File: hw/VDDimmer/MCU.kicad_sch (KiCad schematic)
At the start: 22 parts, among them J1 USB-C 16P, J11 BTN1, J12 BTN2, J13 EXP 3V3/GND/SDA/SCL/EN/IO0, J14 UART1 3V3/GND/TX/RX, U1 ESP32-S3-WROOM-1U-N16

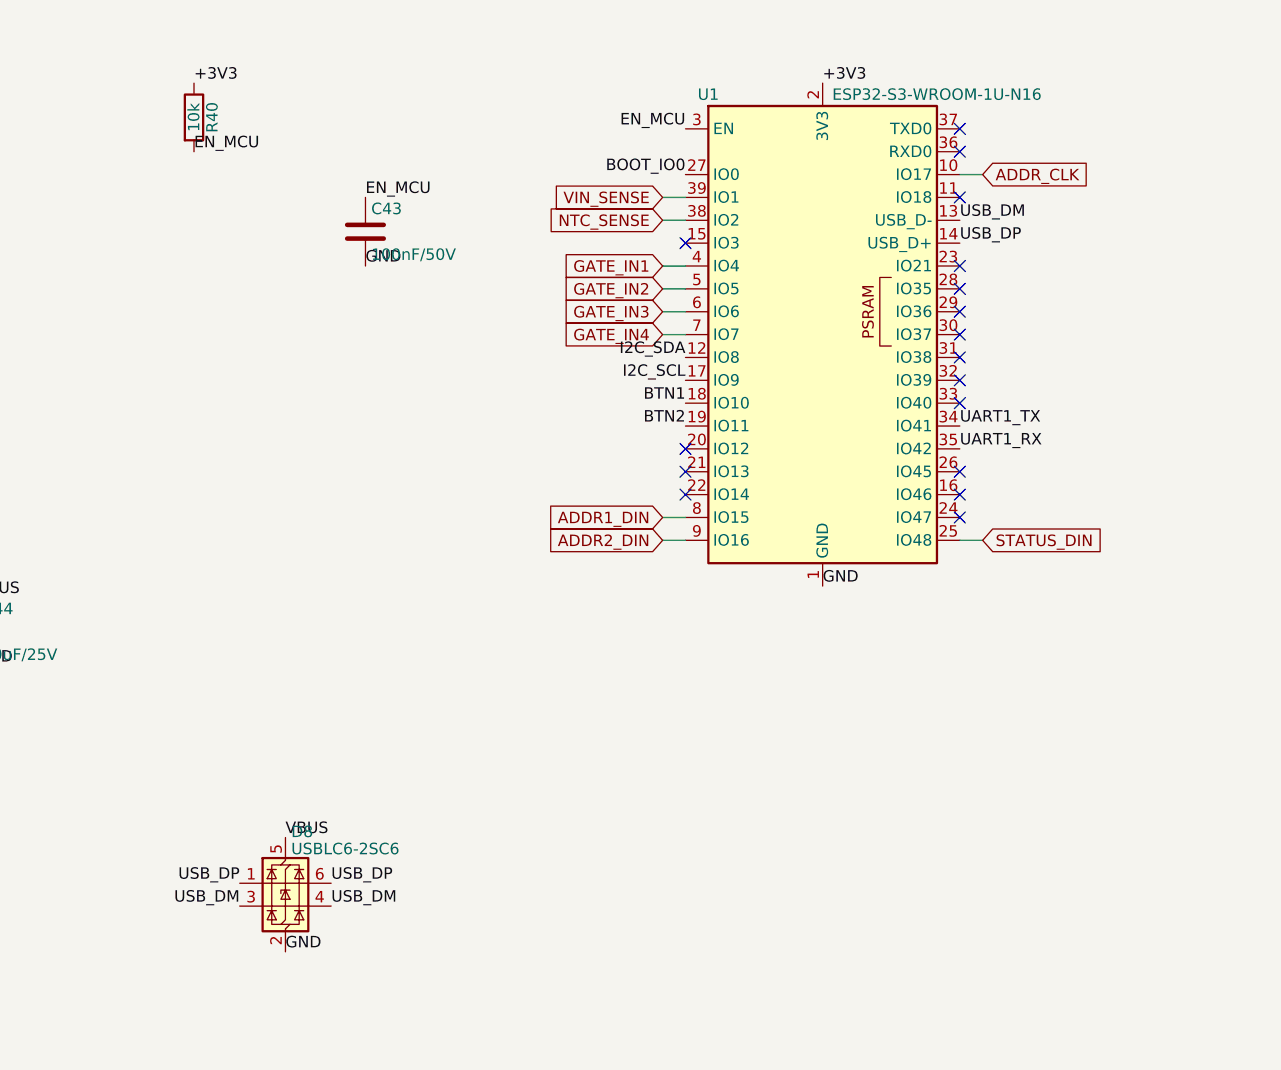
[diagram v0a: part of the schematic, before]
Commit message: Re-pin U1: move 8 nets off the bottom row onto free right-column GPIOs
Measured blocker: the escape from U1's bottom row past x=149.6 has a free
window of y 110.06..113.38 (3.32 mm) = 6 lanes at 0.25 mm trace / 0.2 mm
clearance, plus 3 more reachable via the D3-D4 slot into the corridor above Q4.
Nine eastbound nets left that row (GATE_IN1-4, ADDR1_DIN, ADDR2_DIN, ADDR_CLK,
I2C_SDA, EN_MCU) and four westbound returned through it (GDRV1-4): 13 needed,
9 available. Not routable on 2 layers with B.Cu reserved for GND.

Reassignment (schematic only, no BOM change, firmware-configurable):
  GATE_IN1  IO4  pad4  -> IO3   pad15   y 108.985
  GATE_IN2  IO5  pad5  -> IO46  pad16   y 107.715
  GATE_IN3  IO6  pad6  -> IO12  pad20   y 102.635
  GATE_IN4  IO7  pad7  -> IO13  pad21   y 101.365
  I2C_SDA   IO8  pad12 -> IO14  pad22   y 100.095  (level with J13.3)
  ADDR1_DIN IO15 pad8  -> IO21  pad23   y  98.825
  ADDR2_DIN IO16 pad9  -> IO47  pad24   y  97.555
  ADDR_CLK  IO17 pad10 -> IO45  pad26   y  95.015

Strapping-pin safety: IO45 (VDD_SPI select) and IO46 (ROM print control) both
drive 74HCT125 inputs only, which are high-Z, so their internal pulldowns hold
them low through reset. IO3 (JTAG source select) likewise sees only a high-Z
74HCT125 input, and its strap only selects JTAG routing. I2C_SDA, which may
carry an off-board pull-up via J13, went to IO14 -- not a strapping pin.

Corner load after: GDRV1-4 west (4) + EN_MCU east (1) = 5 of 6 lanes.
ERC 0/0. DRC 0 errors, 0 phantom pads, unconnected 190.

Co-Authored-By: Claude Opus 5 (1M context) <noreply@anthropic.com>
Claude-Session: https://claude.ai/code/session_01XeXr1isxVCg8kRo5Eh8BHM
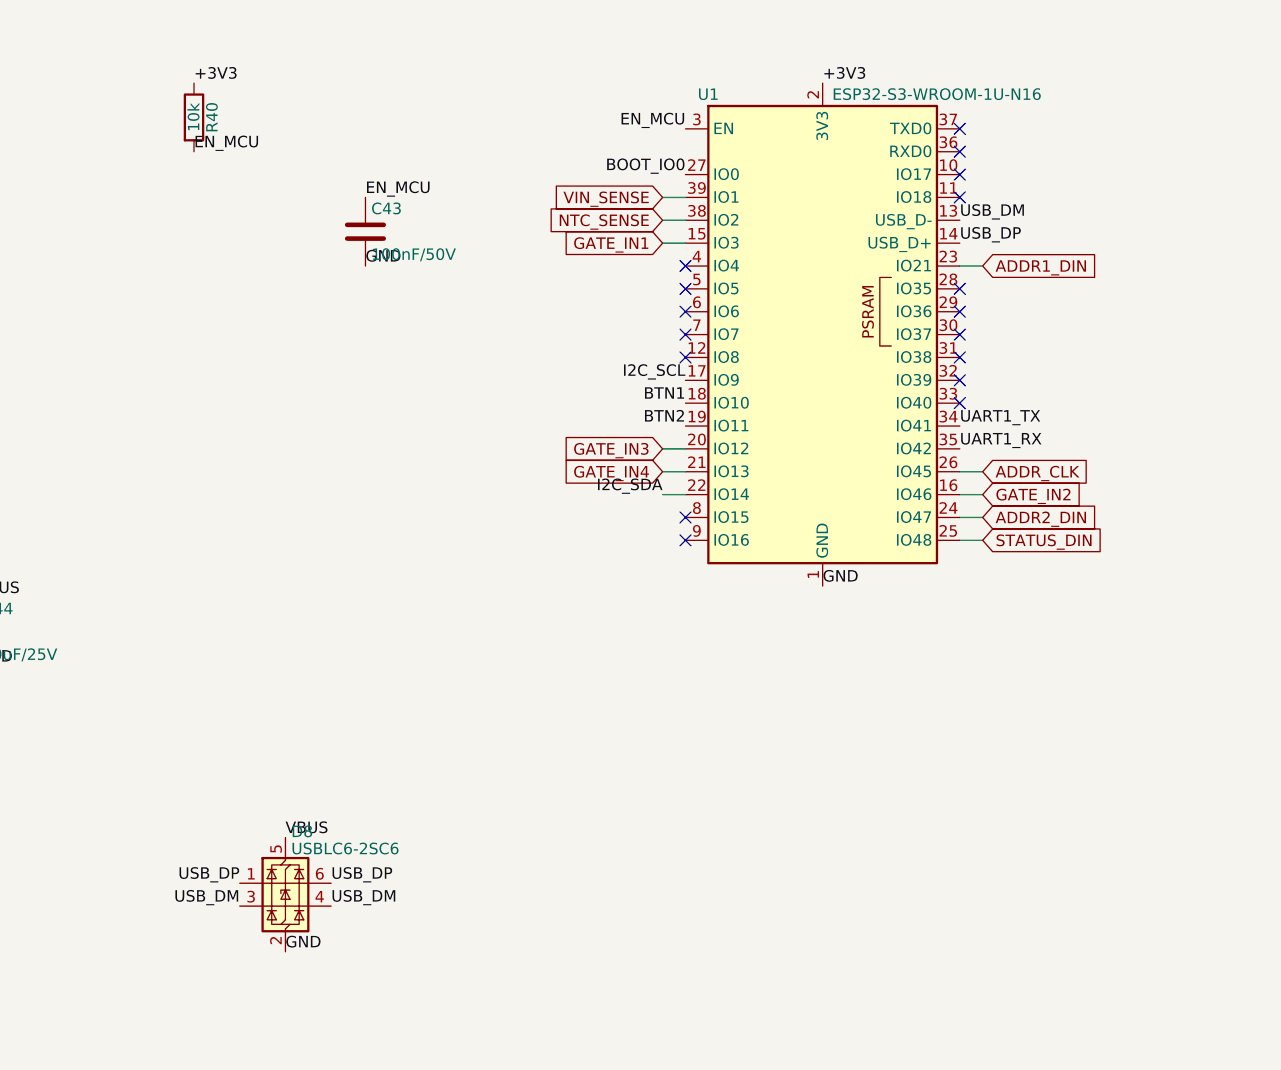
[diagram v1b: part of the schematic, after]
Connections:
- net ADDR1_DIN: now also U1.23 (IO21); no longer U1.8 (IO15)
- net ADDR2_DIN: now also U1.24 (IO47); no longer U1.9 (IO16)
- net ADDR_CLK: now also U1.26 (IO45); no longer U1.10 (IO17)
- net GATE_IN1: now also U1.15 (IO3); no longer U1.4 (IO4)
- net GATE_IN2: now also U1.16 (IO46); no longer U1.5 (IO5)
- net GATE_IN3: now also U1.20 (IO12); no longer U1.6 (IO6)
- net GATE_IN4: now also U1.21 (IO13); no longer U1.7 (IO7)
- net I2C_SDA: now also U1.22 (IO14); no longer U1.12 (IO8)
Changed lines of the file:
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@@
-	)
-	(no_connect
-		(at 184.15 109.22)
-	)
-	(no_connect
-		(at 214.63 137.16)
-	)
-	(no_connect
-		(at 184.15 132.08)
-	)
-	(no_connect
-		(at 184.15 134.62)
-	)
-	(no_connect
-		(at 184.15 137.16)
-	)
-	(no_connect
-		(at 214.63 111.76)
-	)
-	(no_connect
-		(at 214.63 139.7)
-	)
-	(no_connect
-		(at 214.63 134.62)
 	)
 	(no_connect
@@
 	(no_connect
 		(at 59.69 190.5)
+	)
+	(no_connect
+		(at 184.15 111.76)
+	)
+	(no_connect
+		(at 184.15 114.3)
+	)
+	(no_connect
+		(at 184.15 116.84)
+	)
+	(no_connect
+		(at 184.15 119.38)
+	)
+	(no_connect
+		(at 184.15 139.7)
+	)
+	(no_connect
+		(at 184.15 142.24)
+	)
+	(no_connect
+		(at 214.63 101.6)
+	)
+	(no_connect
+		(at 184.15 121.92)
 	)
 	(wire
@@
 	(wire
 		(pts
-			(xy 184.15 111.76)
-			(xy 181.61 111.76)
-		)
-	)
-	(wire
-		(pts
-			(xy 184.15 114.3)
-			(xy 181.61 114.3)
-		)
-	)
-	(wire
-		(pts
-			(xy 184.15 116.84)
-			(xy 181.61 116.84)
-		)
-	)
-	(wire
-		(pts
-			(xy 184.15 119.38)
-			(xy 181.61 119.38)
-		)
-	)
-	(wire
-		(pts
-			(xy 184.15 139.7)
-			(xy 181.61 139.7)
-		)
-	)
-	(wire
-		(pts
-			(xy 184.15 142.24)
-			(xy 181.61 142.24)
-		)
-	)
-	(wire
-		(pts
-			(xy 214.63 101.6)
-			(xy 217.17 101.6)
-		)
-	)
-	(wire
-		(pts
 			(xy 214.63 142.24)
 			(xy 217.17 142.24)
@@
 		)
 	)
+	(wire
+		(pts
+			(xy 184.15 109.22)
+			(xy 181.61 109.22)
+		)
+	)
+	(wire
+		(pts
+			(xy 214.63 137.16)
+			(xy 217.17 137.16)
+		)
+	)
+	(wire
+		(pts
+			(xy 184.15 132.08)
+			(xy 181.61 132.08)
+		)
+	)
+	(wire
+		(pts
+			(xy 184.15 134.62)
+			(xy 181.61 134.62)
+		)
+	)
+	(wire
+		(pts
+			(xy 184.15 137.16)
+			(xy 181.61 137.16)
+		)
+	)
+	(wire
+		(pts
+			(xy 214.63 111.76)
+			(xy 217.17 111.76)
+		)
+	)
+	(wire
+		(pts
+			(xy 214.63 139.7)
+			(xy 217.17 139.7)
+		)
+	)
+	(wire
+		(pts
+			(xy 214.63 134.62)
+			(xy 217.17 134.62)
+		)
+	)
 	(label "+3V3"
 		(at 199.39 91.44 0)
@@
 	)
 	(label "I2C_SDA"
-		(at 184.15 121.92 180)
-		(effects
-			(font
-				(size 1.27 1.27)
-			)
-			(justify right bottom)
-		)
-	)
-	(label "I2C_SDA"
 		(at 294.64 110.49 180)
 		(effects
@@
 		)
 	)
+	(label "USB_DP"
+		(at 134.62 180.34 180)
+		(effects
+			(font
+				(size 1.27 1.27)
+			)
+			(justify right bottom)
+		)
+	)
+	(label "USB_DP"
+		(at 144.78 180.34 0)
+		(effects
+			(font
+				(size 1.27 1.27)
+			)
+			(justify left bottom)
+		)
+	)
+	(label "USB_DM"
+		(at 134.62 182.88 180)
+		(effects
+			(font
+				(size 1.27 1.27)
+			)
+			(justify right bottom)
+		)
+	)
+	(label "USB_DM"
+		(at 144.78 182.88 0)
+		(effects
+			(font
+				(size 1.27 1.27)
+			)
+			(justify left bottom)
+		)
+	)
+	(label "VBUS"
+		(at 139.7 175.26 0)
+		(effects
+			(font
+				(size 1.27 1.27)
+			)
+			(justify left bottom)
+		)
+	)
+	(label "GND"
+		(at 139.7 187.96 0)
+		(effects
+			(font
+				(size 1.27 1.27)
+			)
+			(justify left bottom)
+		)
+	)
+	(label "I2C_SDA"
+		(at 181.61 137.16 180)
+		(effects
+			(font
+				(size 1.27 1.27)
+			)
+			(justify right bottom)
+		)
+	)
+	(global_label "STATUS_DIN"
+		(shape input)
+		(at 217.17 142.24 0)
+		(effects
+			(font
+				(size 1.27 1.27)
+			)
+			(justify left)
+		)
+	)
+	(global_label "VIN_SENSE"
+		(shape input)
+		(at 181.61 104.14 180)
+		(effects
+			(font
+				(size 1.27 1.27)
+			)
+			(justify right)
+		)
+	)
+	(global_label "NTC_SENSE"
+		(shape input)
+		(at 181.61 106.68 180)
+		(effects
+			(font
+				(size 1.27 1.27)
+			)
+			(justify right)
+		)
+	)
 	(global_label "GATE_IN1"
 		(shape input)
-		(at 181.61 111.76 180)
+		(at 181.61 109.22 180)
 		(effects
 			(font
@@
 	(global_label "GATE_IN2"
 		(shape input)
-		(at 181.61 114.3 180)
+		(at 217.17 137.16 0)
+		(effects
+			(font
+				(size 1.27 1.27)
+			)
+			(justify left)
+		)
+	)
+	(global_label "GATE_IN3"
+		(shape input)
+		(at 181.61 132.08 180)
 		(effects
 			(font
@@
 		)
 	)
-	(global_label "GATE_IN3"
-		(shape input)
-		(at 181.61 116.84 180)
+	(global_label "GATE_IN4"
+		(shape input)
+		(at 181.61 134.62 180)
 		(effects
 			(font
@@
 		)
 	)
-	(global_label "GATE_IN4"
-		(shape input)
-		(at 181.61 119.38 180)
-		(effects
-			(font
-				(size 1.27 1.27)
-			)
-			(justify right)
-		)
-	)
 	(global_label "ADDR1_DIN"
 		(shape input)
-		(at 181.61 139.7 180)
-		(effects
-			(font
-				(size 1.27 1.27)
-			)
-			(justify right)
+		(at 217.17 111.76 0)
+		(effects
+			(font
+				(size 1.27 1.27)
+			)
+			(justify left)
 		)
 	)
 	(global_label "ADDR2_DIN"
 		(shape input)
-		(at 181.61 142.24 180)
-		(effects
-			(font
-				(size 1.27 1.27)
-			)
-			(justify right)
+		(at 217.17 139.7 0)
+		(effects
+			(font
+				(size 1.27 1.27)
+			)
+			(justify left)
 		)
 	)
 	(global_label "ADDR_CLK"
 		(shape input)
-		(at 217.17 101.6 0)
+		(at 217.17 134.62 0)
 		(effects
 			(font
@@
 		)
 	)
-	(global_label "STATUS_DIN"
-		(shape input)
-		(at 217.17 142.24 0)
-		(effects
-			(font
-				(size 1.27 1.27)
-			)
-			(justify left)
-		)
-	)
-	(global_label "VIN_SENSE"
-		(shape input)
-		(at 181.61 104.14 180)
-		(effects
-			(font
-				(size 1.27 1.27)
-			)
-			(justify right)
-		)
-	)
-	(global_label "NTC_SENSE"
-		(shape input)
-		(at 181.61 106.68 180)
-		(effects
-			(font
-				(size 1.27 1.27)
-			)
-			(justify right)
-		)
-	)
-  (label "USB_DP"
-    (at 134.61999999999998 180.34 180)
-    (fields_autoplaced yes)
-    (effects (font (size 1.27 1.27)) (justify right bottom))
-  )
-  (label "USB_DP"
-    (at 144.78 180.34 0)
-    (fields_autoplaced yes)
-    (effects (font (size 1.27 1.27)) (justify left bottom))
-  )
-  (label "USB_DM"
-    (at 134.61999999999998 182.88 180)
-    (fields_autoplaced yes)
-    (effects (font (size 1.27 1.27)) (justify right bottom))
-  )
-  (label "USB_DM"
-    (at 144.78 182.88 0)
-    (fields_autoplaced yes)
-    (effects (font (size 1.27 1.27)) (justify left bottom))
-  )
-  (label "VBUS"
-    (at 139.7 175.26 0)
-    (fields_autoplaced yes)
-    (effects (font (size 1.27 1.27)) (justify left bottom))
-  )
-  (label "GND"
-    (at 139.7 187.96 0)
-    (fields_autoplaced yes)
-    (effects (font (size 1.27 1.27)) (justify left bottom))
-  )
 	(symbol
 		(lib_id "RF_Module:ESP32-S3-WROOM-1")

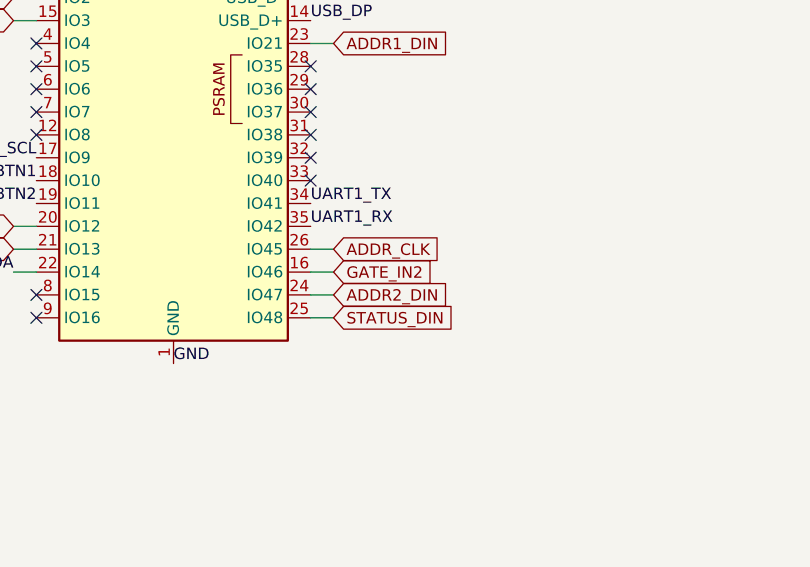
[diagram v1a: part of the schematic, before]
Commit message: Route the addressable section; swap U5 ch3/ch4 and U1's CLK/STATUS pins
Two pin swaps were needed to make the section planar; both are functionally
free and neither changes the BOM:

1. U5 channels 3 and 4 exchanged (A3/Y3 <-> A4/Y4). Both OE pins are tied to
   GND, so the channels are interchangeable. Before the swap STATUS_D5V left
   pin 8 (y=118.41, the southern output) heading north to R13, while
   ADDR_CLK5V left pin 11 (y=114.6, northern) heading south to R11/R12 -- a
   forced crossing. After the swap each output leaves on the side its load is
   on.
2. U1's ADDR_CLK and STATUS_DIN exchanged (IO45 pad26 <-> IO48 pad25). The
   ch3/ch4 swap inverted the required order at U5's inputs; moving the two
   source pins restores north-source-to-north-pad ordering.

U5's four inputs descend the SOIC body gap on lanes x = 168.6/169.1/170.1/170.6
-- the same trick used on U4 -- which frees both pad columns for the outputs.

Re-placement: R9/R11 moved from the x 175..181 cluster to x 156.5/161.5 beside
J7, R10/R12 to x 173.5/177 beside J8, all at y=125.0; R13 to (177,117).
Previously all five sat 15-20 mm from the connectors they feed. C34 moved to
(172,90) to clear the STATUS_DIN lane at y=92.0 (was 0.025 mm).
PF1/PF2 rotated 180 so V+SEL faces J9/J10 (east) and VOUT faces the JSTs
(west); this turned two wrapping nets into single L-bends.

Bottom-layer copper: one 1.25 mm B.Cu hop on ADDR2_D5V at x=172.588, y
122.775..124.025 (two 0.6/0.3 mm vias), where it must cross the ADDR_CLK5V
bus that straddles it. ADDR_CLK5V feeds R11 (x=160.6) and R12 (x=176.1) with
R10's feed at x=172.6 between them, so one crossing is topologically forced.
The cut in the bottom GND pour is 1.25 x 0.6 mm at 78 mm from the buck; the
8.5.3 keepout region is untouched.

DRC 0 errors, 0 phantom pads, unconnected 166 -> 146.

Co-Authored-By: Claude Opus 5 (1M context) <noreply@anthropic.com>
Claude-Session: https://claude.ai/code/session_01XeXr1isxVCg8kRo5Eh8BHM
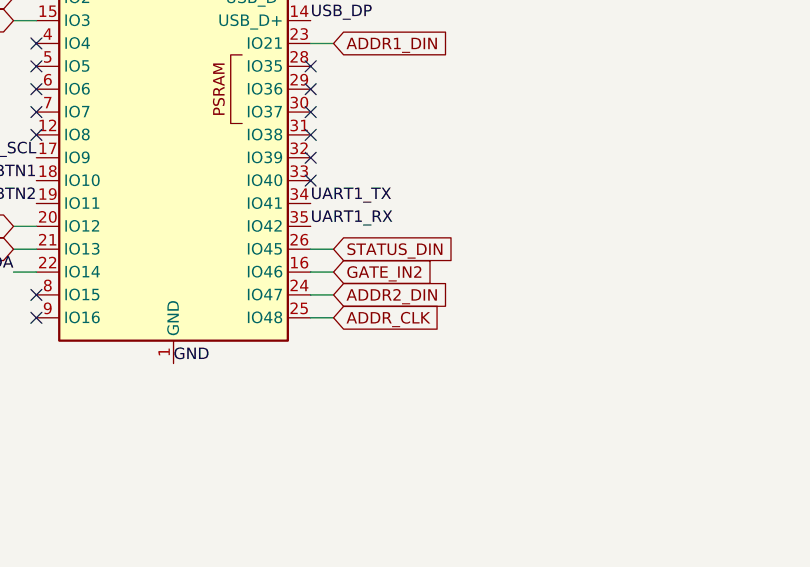
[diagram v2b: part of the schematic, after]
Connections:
- net ADDR_CLK: now also U1.25 (IO48); no longer U1.26 (IO45)
- net STATUS_DIN: now also U1.26 (IO45); no longer U1.25 (IO48)
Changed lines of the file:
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@@
-		)
-	)
-	(global_label "STATUS_DIN"
-		(shape input)
-		(at 217.17 142.24 0)
-		(effects
-			(font
-				(size 1.27 1.27)
-			)
-			(justify left)
 		)
 	)
@@
 		)
 	)
-	(global_label "ADDR_CLK"
+	(global_label "STATUS_DIN"
 		(shape input)
 		(at 217.17 134.62 0)
 		(effects
 			(font
+				(size 1.27 1.27)
+			)
+			(justify left)
+		)
+	)
+	(global_label "ADDR_CLK"
+		(shape input)
+		(at 217.17 142.24 0)
+		(effects
+			(font
